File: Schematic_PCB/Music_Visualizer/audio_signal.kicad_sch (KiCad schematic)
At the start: 13 parts, among them J1 NMJ4HCD2, J3 Screw_Terminal_01x02, J4 NMJ4HCD2, J5 Screw_Terminal_01x02, U2 LM324, U3 LM324

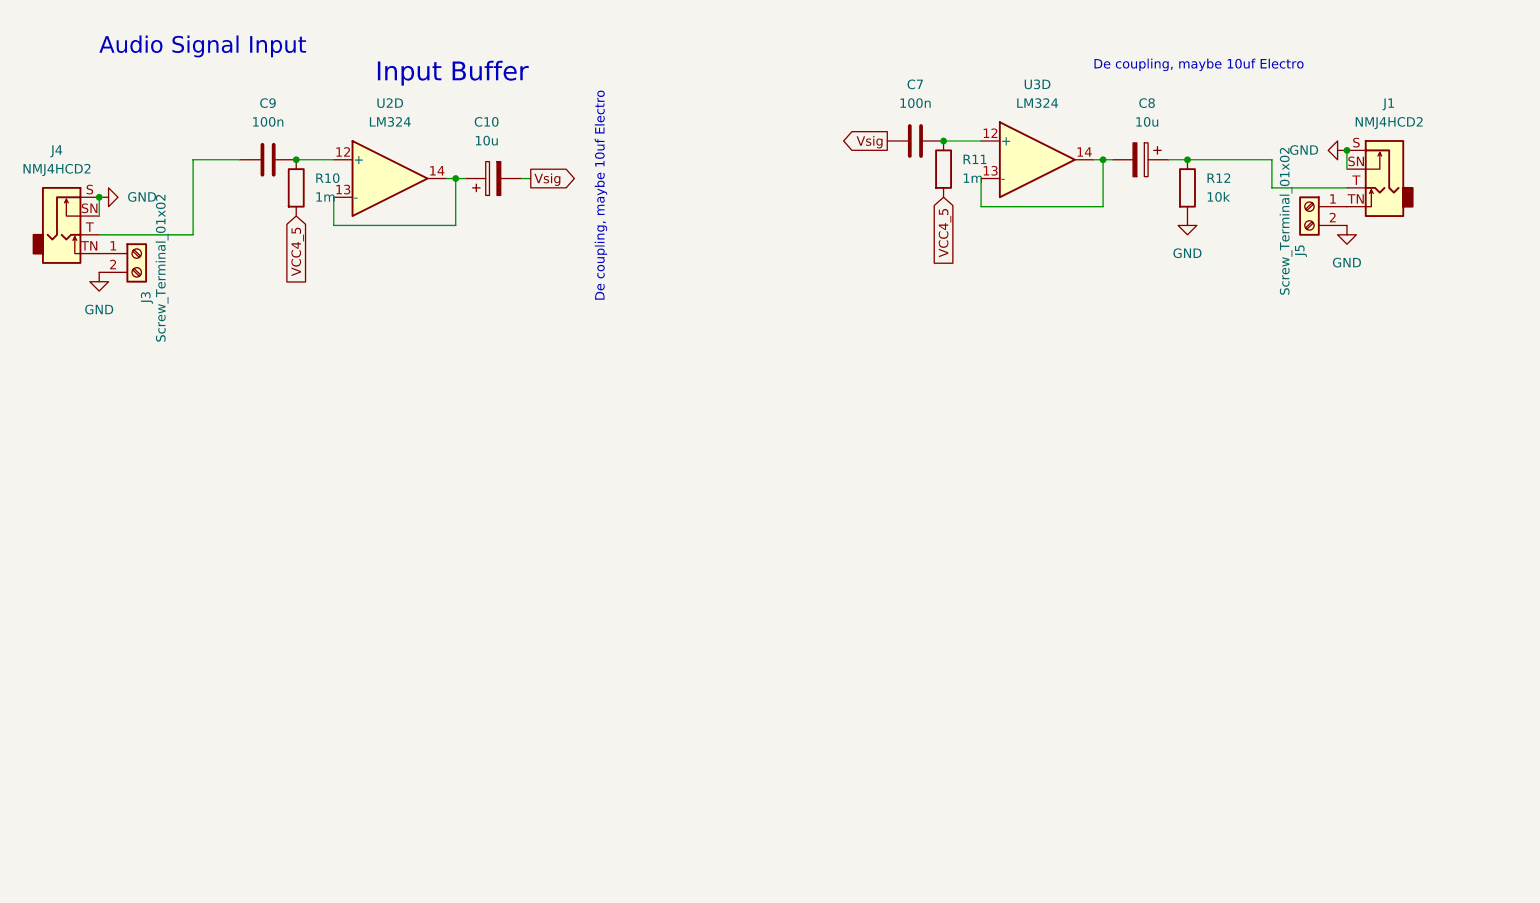
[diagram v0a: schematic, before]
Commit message: Add testpoints
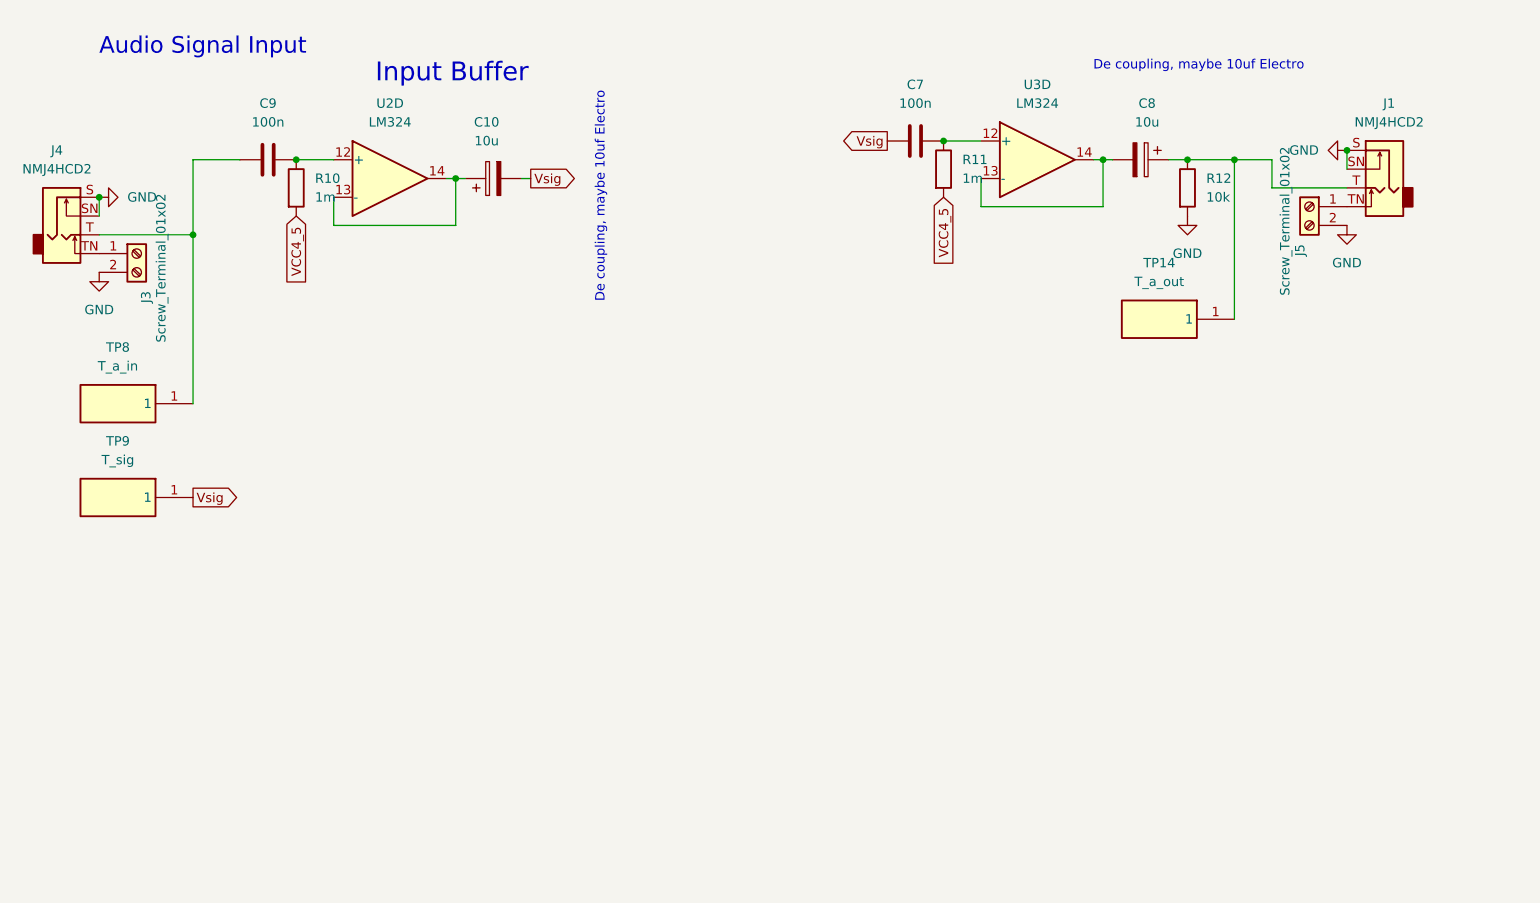
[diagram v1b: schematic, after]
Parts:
- added TP14: T_a_out, Custom_Footprints:TEST1Y, symbol TEST-1_Y_:TEST-1_Y_
- added TP8: T_a_in, Custom_Footprints:TEST1Y, symbol TEST-1_Y_:TEST-1_Y_
- added TP9: T_sig, Custom_Footprints:TEST1Y, symbol TEST-1_Y_:TEST-1_Y_
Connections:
- net Vsig: now also TP9.1
- net at C8.1, J1.T, R12.1: now also TP14.1
- net at C9.1, J4.T: now also TP8.1

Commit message: In-Out switch
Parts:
- added SW1: SW_Slide_DPDT, Button_Switch_THT:SW_CK_JS202011CQN_DPDT_Straight, symbol Switch:SW_Slide_DPDT
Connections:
- net at C8.1, R12.1, TP14.1: now also SW1.5 (B); no longer J1.T
- net at C9.1, TP8.1: now also SW1.2 (B); no longer J4.T
- new net Left jack: J4.T, SW1.1 (A), SW1.4 (A)
- new net Right jack: J1.T, SW1.3 (C), SW1.6 (C)
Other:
- note added: "Input - Output switch"
- note added: "Left jack"
- note added: "Output Buffer"
- note added: "Right Jack"
- note removed: "Audio Signal Input"
- note removed: "De coupling, maybe 10uf Electro"
- moved on the sheet: C10, C7, C8, C9, J3, J4, R10, R11, R12, TP14, TP8, U2D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

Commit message: Correct op amps
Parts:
- added R85: 100, Resistor_SMD:R_0805_2012Metric_Pad1.20x1.40mm_HandSolder, symbol Device:R
- added unit 3 of U8
- R12: value 10k -> 100k
- renumbered U2 to U8, U3 to U8
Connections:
- net VCC4_5: now also U8.10 (+)
- net at C7.2, R11.1: now also U8.5 (+); no longer U8.12 (+)
- net at C9.2, R10.1: now also U8.3 (+); no longer U8.12 (+)
- new net: C8.2, R85.2
- new net: C10.1, U8.1, U8.2 (-)
- new net: R85.1, U8.6 (-), U8.7
- new net: U8.8, U8.9 (-)
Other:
- note added: "Parked"
- moved on the sheet: C7, C8, R11, R12, U8B

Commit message: Battery low
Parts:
- J1, J4: footprint Connector_Audio:Jack_6.35mm_Neutrik_NMJ4HCD2_Horizontal -> Custom_Footprints:Jack_6.35mm
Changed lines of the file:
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@@
 			)
 		)
-		(property "Footprint" "Connector_Audio:Jack_6.35mm_Neutrik_NMJ4HCD2_Horizontal"
+		(property "Footprint" "Custom_Footprints:Jack_6.35mm"
 			(at 212.09 44.45 0)
 			(effects
@@
 			)
 		)
-		(property "Footprint" "Connector_Audio:Jack_6.35mm_Neutrik_NMJ4HCD2_Horizontal"
+		(property "Footprint" "Custom_Footprints:Jack_6.35mm"
 			(at 41.91 44.45 0)
 			(effects

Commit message: PCB V1 done
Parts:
- C7, C9: footprint Capacitor_SMD:C_0805_2012Metric_Pad1.18x1.45mm_HandSolder -> Custom_Footprints:C_0805_2012Metric_Pad1.18x1.45mm_HandSolder
- R10, R11, R12, R85: footprint Resistor_SMD:R_0805_2012Metric_Pad1.20x1.40mm_HandSolder -> Custom_Footprints:R_0805_2012Metric_Pad1.20x1.40mm_HandSolder
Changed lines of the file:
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@@
 			)
 		)
-		(property "Footprint" "Resistor_SMD:R_0805_2012Metric_Pad1.20x1.40mm_HandSolder"
+		(property "Footprint" "Custom_Footprints:R_0805_2012Metric_Pad1.20x1.40mm_HandSolder"
 			(at 98.552 129.54 90)
 			(effects
@@
 					(size 1.27 1.27)
 				)
+			)
+		)
+		(property "STANDART" ""
+			(at 100.33 129.54 0)
+			(effects
+				(font
+					(size 1.27 1.27)
+				)
+				(hide yes)
 			)
 		)
@@
 			)
 		)
-		(property "Footprint" "Capacitor_SMD:C_0805_2012Metric_Pad1.18x1.45mm_HandSolder"
+		(property "Footprint" "Custom_Footprints:C_0805_2012Metric_Pad1.18x1.45mm_HandSolder"
 			(at 100.33 124.7648 0)
 			(effects
@@
 					(size 1.27 1.27)
 				)
+			)
+		)
+		(property "STANDART" ""
+			(at 96.52 125.73 90)
+			(effects
+				(font
+					(size 1.27 1.27)
+				)
+				(hide yes)
 			)
 		)
@@
 					(size 1.27 1.27)
 				)
+			)
+		)
+		(property "STANDART" ""
+			(at 138.43 128.27 90)
+			(effects
+				(font
+					(size 1.27 1.27)
+				)
+				(hide yes)
 			)
 		)
@@
 			)
 		)
+		(property "STANDART" ""
+			(at 118.11 46.99 0)
+			(effects
+				(font
+					(size 1.27 1.27)
+				)
+				(hide yes)
+			)
+		)
 		(pin "1"
 		)
@@
 				)
 				(justify left top)
+				(hide yes)
+			)
+		)
+		(property "STANDART" ""
+			(at 148.59 128.27 0)
+			(effects
+				(font
+					(size 1.27 1.27)
+				)
 				(hide yes)
 			)
@@
 			)
 		)
+		(property "STANDART" ""
+			(at 201.93 52.07 90)
+			(effects
+				(font
+					(size 1.27 1.27)
+				)
+				(hide yes)
+			)
+		)
 		(pin "1"
 		)
@@
 			)
 		)
+		(property "STANDART" ""
+			(at 132.08 46.99 90)
+			(effects
+				(font
+					(size 1.27 1.27)
+				)
+				(hide yes)
+			)
+		)
 		(pin "1"
 		)
@@
 			)
 		)
+		(property "STANDART" ""
+			(at 113.03 128.27 0)
+			(effects
+				(font
+					(size 1.27 1.27)
+				)
+				(hide yes)
+			)
+		)
 		(pin "1"
 		)
@@
 			)
 		)
-		(property "Footprint" "Resistor_SMD:R_0805_2012Metric_Pad1.20x1.40mm_HandSolder"
+		(property "Footprint" "Custom_Footprints:R_0805_2012Metric_Pad1.20x1.40mm_HandSolder"
 			(at 103.632 48.26 90)
 			(effects
@@
 					(size 1.27 1.27)
 				)
+			)
+		)
+		(property "STANDART" ""
+			(at 105.41 48.26 0)
+			(effects
+				(font
+					(size 1.27 1.27)
+				)
+				(hide yes)
 			)
 		)
@@
 			)
 		)
+		(property "STANDART" ""
+			(at 223.52 123.19 0)
+			(effects
+				(font
+					(size 1.27 1.27)
+				)
+				(hide yes)
+			)
+		)
 		(pin "1"
 		)
@@
 		)
 		(property "Description" "Slide Switch, dual pole double throw"
+			(at 128.27 86.36 0)
+			(effects
+				(font
+					(size 1.27 1.27)
+				)
+				(hide yes)
+			)
+		)
+		(property "STANDART" ""
 			(at 128.27 86.36 0)
 			(effects
@@
 			)
 		)
-		(property "Footprint" "Capacitor_SMD:C_0805_2012Metric_Pad1.18x1.45mm_HandSolder"
+		(property "Footprint" "Custom_Footprints:C_0805_2012Metric_Pad1.18x1.45mm_HandSolder"
 			(at 105.41 43.4848 0)
 			(effects
@@
 					(size 1.27 1.27)
 				)
+			)
+		)
+		(property "STANDART" ""
+			(at 101.6 44.45 90)
+			(effects
+				(font
+					(size 1.27 1.27)
+				)
+				(hide yes)
 			)
 		)
@@
 			)
 		)
-		(property "Footprint" "Resistor_SMD:R_0805_2012Metric_Pad1.20x1.40mm_HandSolder"
+		(property "Footprint" "Custom_Footprints:R_0805_2012Metric_Pad1.20x1.40mm_HandSolder"
 			(at 128.27 130.048 90)
 			(effects
@@
 					(size 1.27 1.27)
 				)
+			)
+		)
+		(property "STANDART" ""
+			(at 128.27 128.27 90)
+			(effects
+				(font
+					(size 1.27 1.27)
+				)
+				(hide yes)
 			)
 		)
@@
 			)
 		)
+		(property "STANDART" ""
+			(at 212.09 49.53 0)
+			(effects
+				(font
+					(size 1.27 1.27)
+				)
+				(hide yes)
+			)
+		)
 		(pin "S"
 		)
@@
 			)
 		)
-		(property "Footprint" "Resistor_SMD:R_0805_2012Metric_Pad1.20x1.40mm_HandSolder"
+		(property "Footprint" "Custom_Footprints:R_0805_2012Metric_Pad1.20x1.40mm_HandSolder"
 			(at 143.002 132.08 90)
 			(effects
@@
 					(size 1.27 1.27)
 				)
+			)
+		)
+		(property "STANDART" ""
+			(at 144.78 132.08 0)
+			(effects
+				(font
+					(size 1.27 1.27)
+				)
+				(hide yes)
 			)
 		)
@@
 			)
 		)
+		(property "STANDART" ""
+			(at 52.07 52.07 90)
+			(effects
+				(font
+					(size 1.27 1.27)
+				)
+				(hide yes)
+			)
+		)
 		(pin "1"
 		)
@@
 		)
 		(property "Description" "M Series, 6.35mm (1/4in) mono jack, switched, with chrome ferrule and straight PCB pins"
+			(at 41.91 49.53 0)
+			(effects
+				(font
+					(size 1.27 1.27)
+				)
+				(hide yes)
+			)
+		)
+		(property "STANDART" ""
 			(at 41.91 49.53 0)
 			(effects
@@
 			)
 		)
+		(property "STANDART" ""
+			(at 96.52 44.45 0)
+			(effects
+				(font
+					(size 1.27 1.27)
+				)
+				(hide yes)
+			)
+		)
 		(pin "1"
 		)
@@
 				(hide yes)
 			)
+		)
+		(property "STANDART" ""
+			(at 50.8 91.44 0)
+			(effects
+				(font
+					(size 1.27 1.27)
+				)
+				(hide yes)
+			)

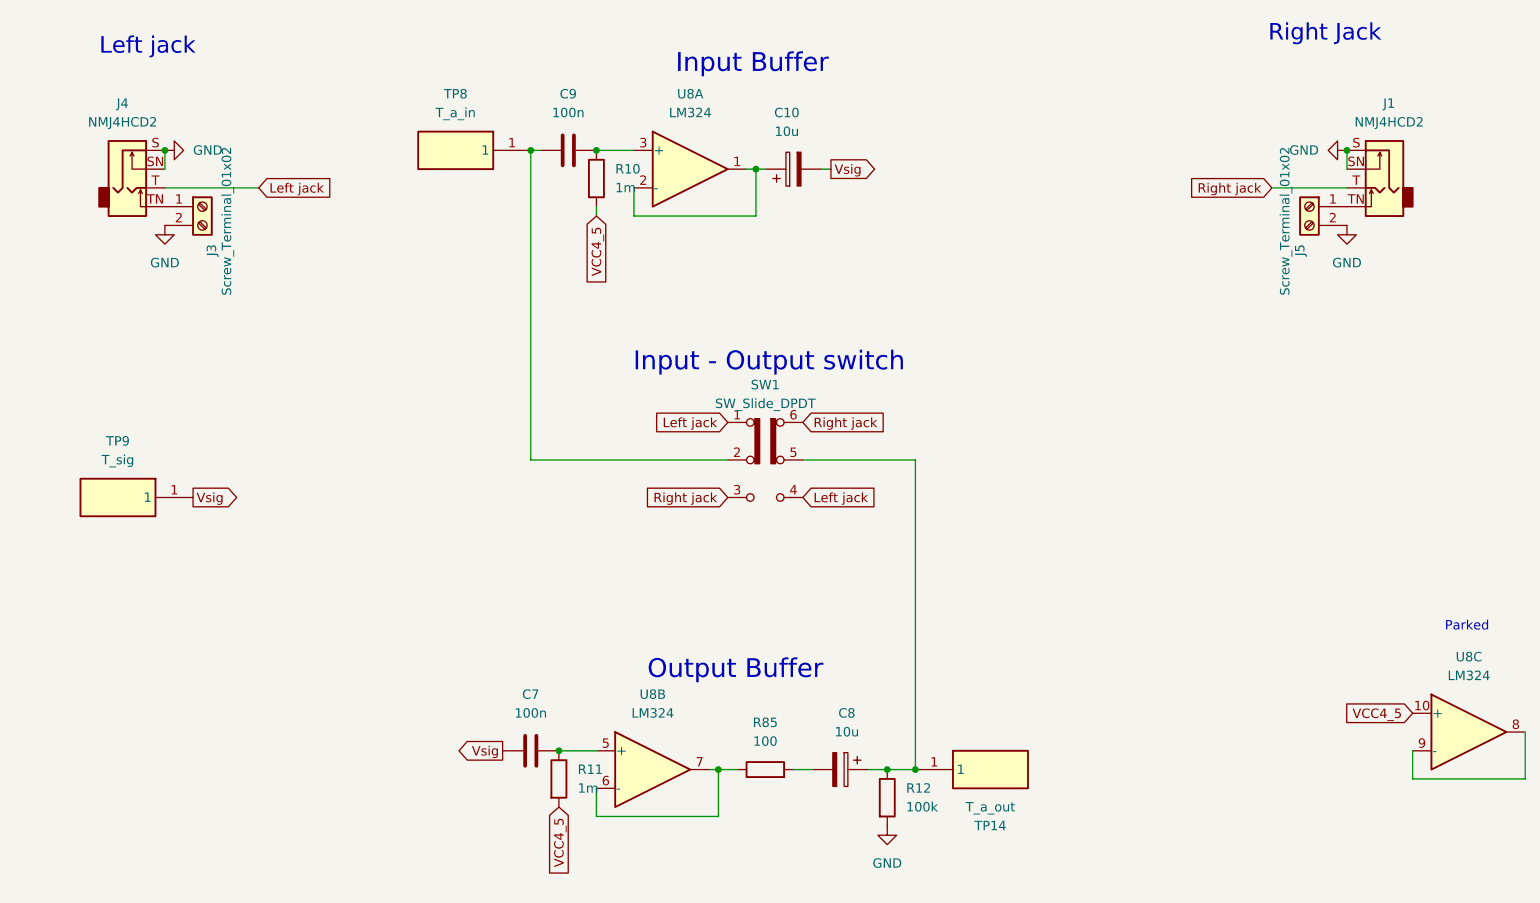
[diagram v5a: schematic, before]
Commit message: Remove jacks and compact placement
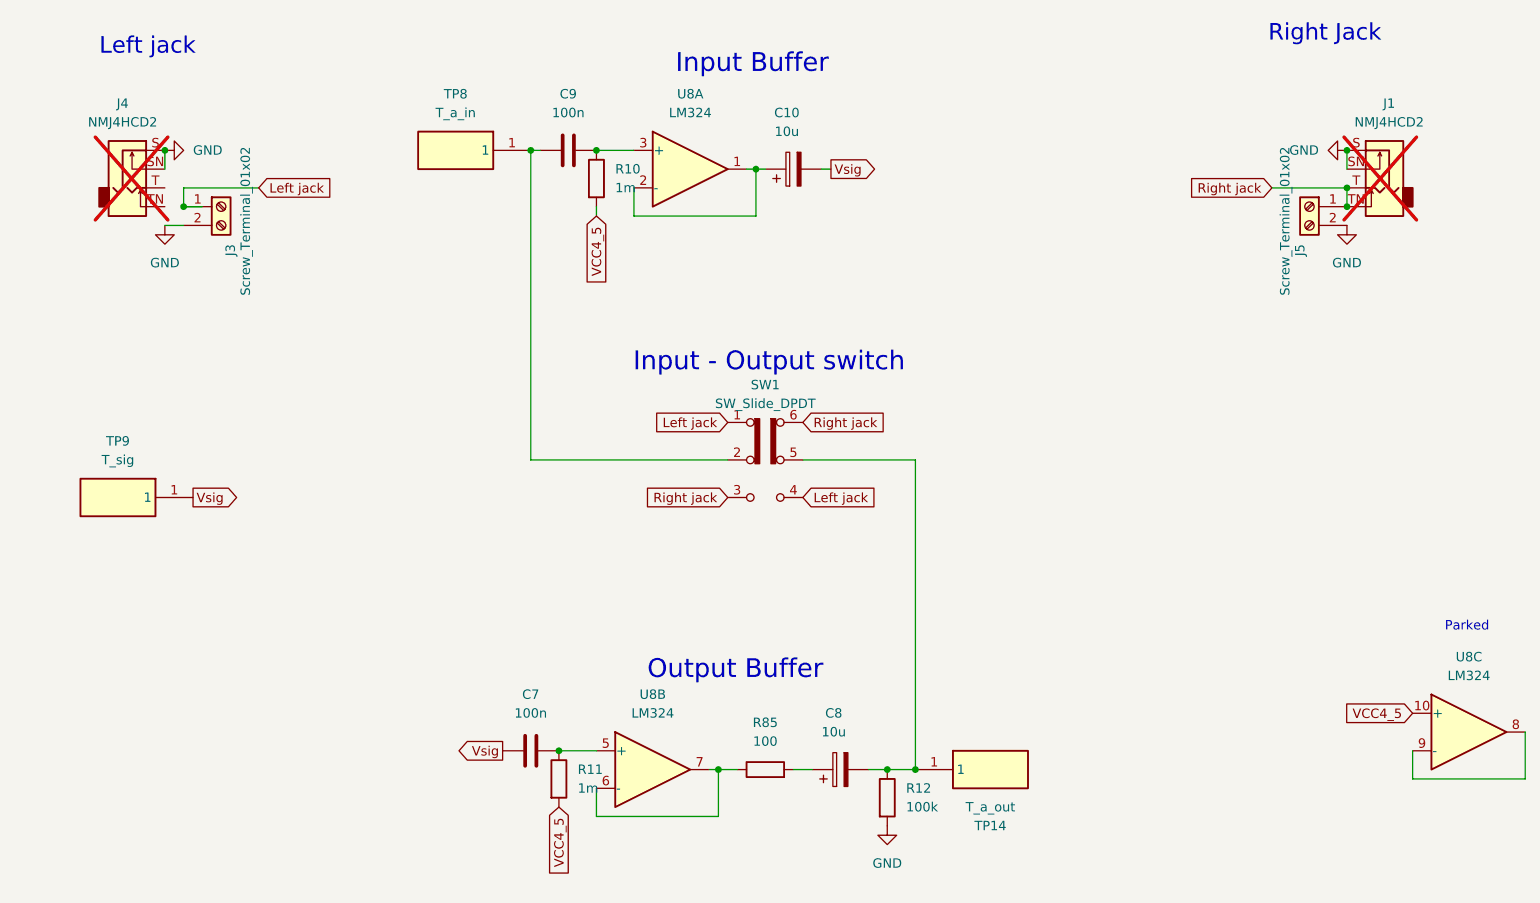
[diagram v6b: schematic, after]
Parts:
- J1, J4: now not fitted; now left out of the parts list
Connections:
- net Left jack: now also J3.1 (Pin_1); no longer J4.T
- net Right jack: now also J1.TN, J5.1 (Pin_1)
- net at R12.1, SW1.5 (B), TP14.1: now also C8.2; no longer C8.1
- net at R85.2: now also C8.1; no longer C8.2
- net at J4.TN: no longer J3.1 (Pin_1)
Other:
- moved on the sheet: C8, J3
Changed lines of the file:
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@@
+	)
+	(junction
+		(at 49.53 52.07)
+		(diameter 0)
+		(color 0 0 0 0)
 	)
 	(junction
@@
 	)
 	(junction
+		(at 207.01 52.07)
+		(diameter 0)
+		(color 0 0 0 0)
+	)
+	(junction
 		(at 100.33 125.73)
 		(diameter 0)
@@
 	)
 	(junction
+		(at 207.01 49.53)
+		(diameter 0)
+		(color 0 0 0 0)
+	)
+	(junction
 		(at 144.78 128.27)
 		(diameter 0)
@@
 	(wire
 		(pts
+			(xy 49.53 52.07) (xy 52.07 52.07)
+		)
+		(stroke
+			(width 0)
+			(type default)
+		)
+	)
+	(wire
+		(pts
 			(xy 207.01 44.45) (xy 207.01 46.99)
 		)
@@
 	(wire
 		(pts
-			(xy 46.99 49.53) (xy 59.69 49.53)
+			(xy 49.53 54.61) (xy 46.99 54.61)
 		)
 		(stroke
@@
 	(wire
 		(pts
+			(xy 207.01 49.53) (xy 207.01 52.07)
+		)
+		(stroke
+			(width 0)
+			(type default)
+		)
+	)
+	(wire
+		(pts
 			(xy 100.33 125.73) (xy 105.41 125.73)
 		)
@@
 	(wire
 		(pts
+			(xy 49.53 49.53) (xy 49.53 52.07)
+		)
+		(stroke
+			(width 0)
+			(type default)
+		)
+	)
+	(wire
+		(pts
 			(xy 105.41 52.07) (xy 105.41 53.34)
 		)
@@
 		(pts
 			(xy 215.9 129.54) (xy 215.9 125.73)
+		)
+		(stroke
+			(width 0)
+			(type default)
+		)
+	)
+	(wire
+		(pts
+			(xy 49.53 49.53) (xy 59.69 49.53)
 		)
 		(stroke
@@
 	(symbol
 		(lib_id "Device:C_Polarized")
-		(at 138.43 128.27 270)
+		(at 138.43 128.27 90)
 		(unit 1)
 		(exclude_from_sim no)
@@
 		(fields_autoplaced yes)
 		(property "Reference" "C8"
-			(at 139.319 120.65 90)
+			(at 137.541 120.65 90)
 			(effects
 				(font
@@
 		)
 		(property "Value" "10u"
-			(at 139.319 123.19 90)
+			(at 137.541 123.19 90)
 			(effects
 				(font
@@
 		)
 		(property "Footprint" "Capacitor_THT:CP_Radial_D5.0mm_P2.00mm"
-			(at 134.62 129.2352 0)
+			(at 142.24 127.3048 0)
 			(effects
 				(font
@@
 		(unit 1)
 		(exclude_from_sim no)
-		(in_bom yes)
-		(on_board yes)
-		(dnp no)
+		(in_bom no)
+		(on_board no)
+		(dnp yes)
 		(fields_autoplaced yes)
 		(property "Reference" "J1"
@@
 	(symbol
 		(lib_id "Connector:Screw_Terminal_01x02")
-		(at 52.07 52.07 0)
+		(at 54.61 52.07 0)
 		(unit 1)
 		(exclude_from_sim no)
@@
 		(dnp no)
 		(property "Reference" "J3"
-			(at 53.3401 57.15 90)
+			(at 55.8801 57.15 90)
 			(effects
 				(font
@@
 		)
 		(property "Value" "Screw_Terminal_01x02"
-			(at 55.372 43.942 90)
+			(at 57.912 43.942 90)
 			(effects
 				(font
@@
 		)
 		(property "Footprint" "TerminalBlock_Phoenix:TerminalBlock_Phoenix_MPT-0,5-2-2.54_1x02_P2.54mm_Horizontal"
-			(at 52.07 52.07 0)
+			(at 54.61 52.07 0)
 			(effects
 				(font
@@
 		)
 		(property "Datasheet" "~"
-			(at 52.07 52.07 0)
+			(at 54.61 52.07 0)
 			(effects
 				(font
@@
 		)
 		(property "Description" ""
-			(at 52.07 52.07 0)
+			(at 54.61 52.07 0)
 			(effects
 				(font
@@
 		)
 		(property "STANDART" ""
-			(at 52.07 52.07 90)
+			(at 54.61 52.07 90)
 			(effects
 				(font
@@
 		(unit 1)
 		(exclude_from_sim no)
-		(in_bom yes)
-		(on_board yes)
-		(dnp no)
+		(in_bom no)
+		(on_board no)
+		(dnp yes)
 		(fields_autoplaced yes)
 		(property "Reference" "J4"
